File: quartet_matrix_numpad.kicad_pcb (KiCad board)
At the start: 2 copper layers, 100 x 100 mm, 34 parts

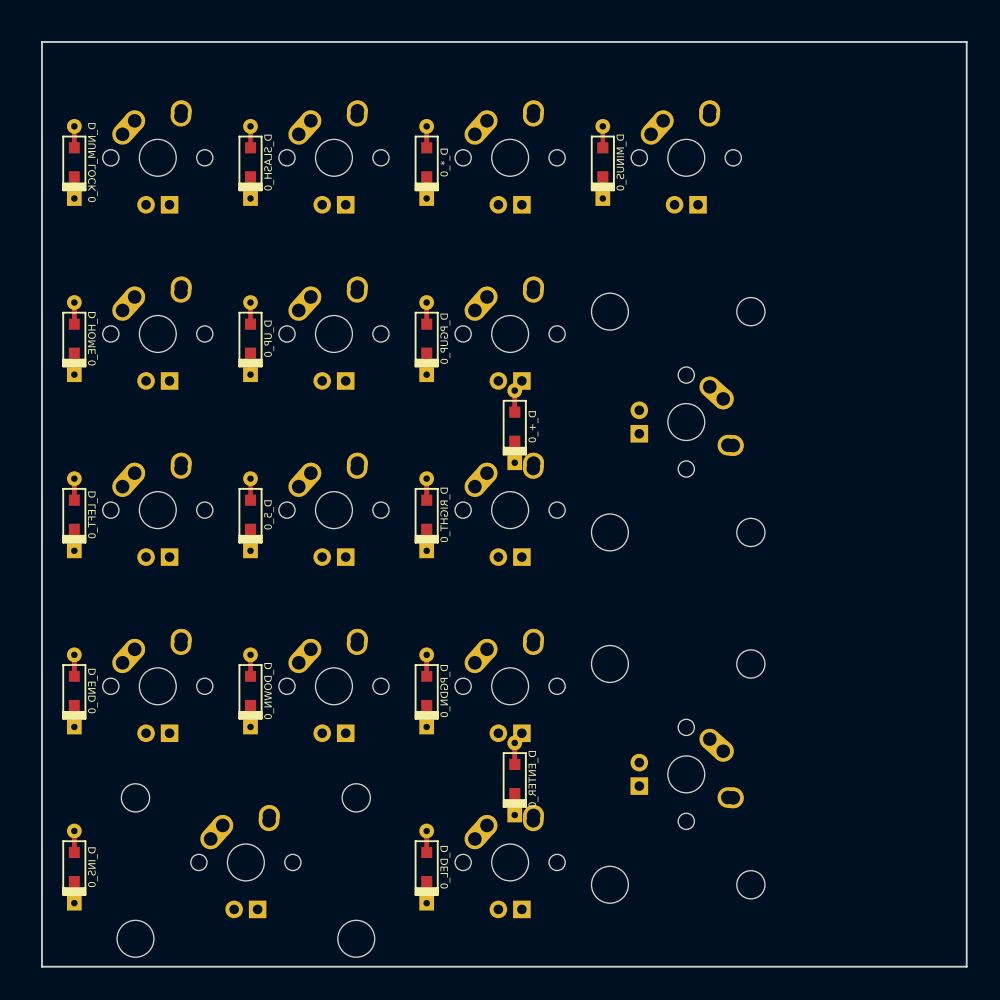
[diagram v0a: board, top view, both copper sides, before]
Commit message: Layout and route numpad matrix
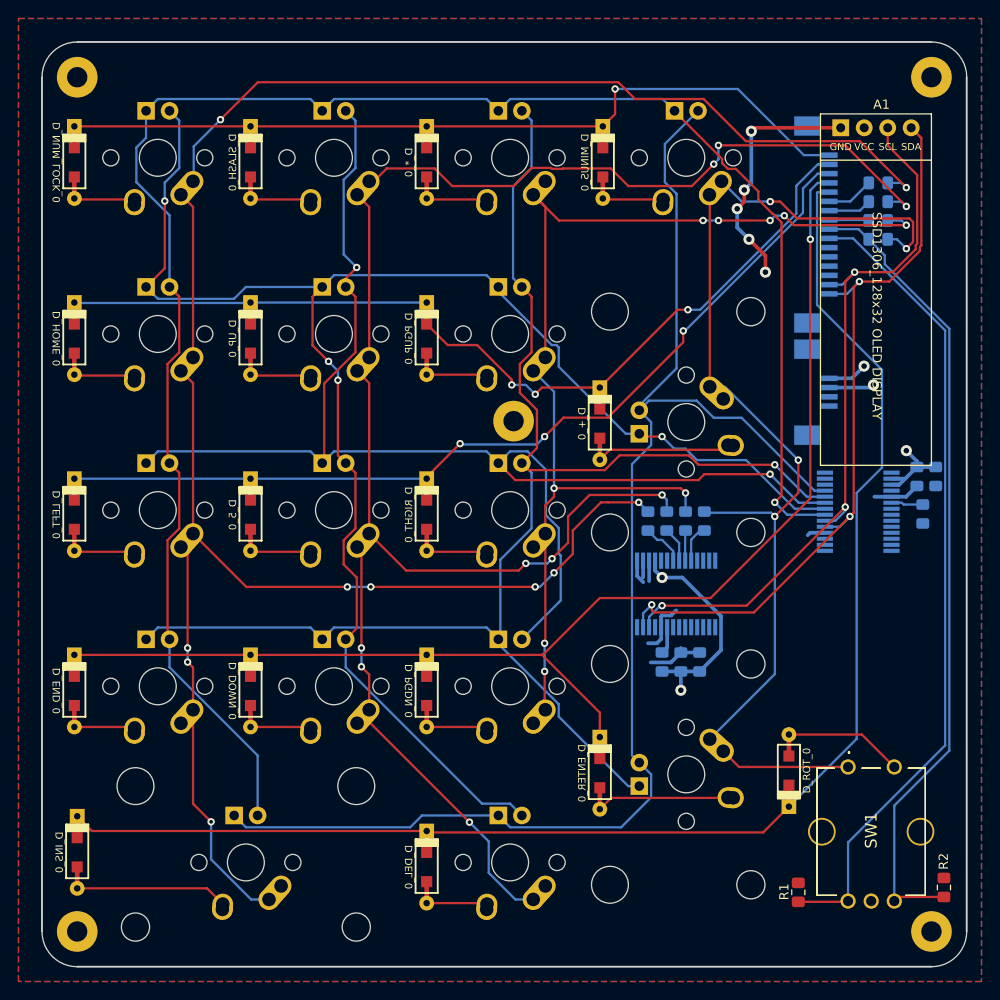
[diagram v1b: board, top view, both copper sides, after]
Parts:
- added A1: SSD1306_I2C_MODULE, Gigahawk:SSD1306_MODULE_128x32, F.Cu at (84.2, 7.78)
- added C1: 1u, Capacitor_SMD:C_0805_2012Metric_Pad1.15x1.40mm_HandSolder, B.Cu at (69.1, 67.0)
- added C2: 0.1u, Capacitor_SMD:C_0805_2012Metric_Pad1.15x1.40mm_HandSolder, B.Cu at (71.1, 67.0)
- added C3: 1u, Capacitor_SMD:C_0805_2012Metric_Pad1.15x1.40mm_HandSolder, B.Cu at (96.6, 47.0)
- added C4: 0.1u, Capacitor_SMD:C_0805_2012Metric_Pad1.15x1.40mm_HandSolder, B.Cu at (94.6, 47.0)
- added D_ROT_0: D, keyboard_parts:D_SOD123_axial, F.Cu at (80.8, 78.8)
- added H1: TopLeft(3.81,3.81), MountingHole:MountingHole_2.2mm_M2_Pad, F.Cu at (3.81, 3.81)
- added H2: TopRight(96.19,3.81), MountingHole:MountingHole_2.2mm_M2_Pad, F.Cu at (96.2, 3.81)
- added H3: BottomLeft(3.81,96.19), MountingHole:MountingHole_2.2mm_M2_Pad, F.Cu at (3.81, 96.2)
- added H4: BottomRight(96.19,96.19), MountingHole:MountingHole_2.2mm_M2_Pad, F.Cu at (96.2, 96.2)
- added H5: Center(51,41), MountingHole:MountingHole_2.2mm_M2_Pad, F.Cu at (51.0, 41.0)
- added H6: ConnectorPos(85.09,39.37), Gigahawk:DOT, F.Cu at (85.1, 39.4)
- added J2: QUARTET_RECV, Gigahawk:QUARTET_RECV_MATRIX, B.Cu at (85.1, 39.4)
- added R1: 20k, Resistor_SMD:R_0805_2012Metric_Pad1.15x1.40mm_HandSolder, F.Cu at (81.8, 92.0)
- added R10: DNI, Resistor_SMD:R_0805_2012Metric_Pad1.15x1.40mm_HandSolder, B.Cu at (90.4, 19.3)
- added R11: DNI, Resistor_SMD:R_0805_2012Metric_Pad1.15x1.40mm_HandSolder, B.Cu at (90.4, 21.3)
- added R12: 20k, Resistor_SMD:R_0805_2012Metric_Pad1.15x1.40mm_HandSolder, B.Cu at (95.2, 51.0)
- added R2: 20k, Resistor_SMD:R_0805_2012Metric_Pad1.15x1.40mm_HandSolder, F.Cu at (97.5, 91.4)
- added R3: 0R, Resistor_SMD:R_0805_2012Metric_Pad1.15x1.40mm_HandSolder, B.Cu at (67.1, 67.0)
- added R4: 0R, Resistor_SMD:R_0805_2012Metric_Pad1.15x1.40mm_HandSolder, B.Cu at (65.5, 51.8)
- added R5: 0R, Resistor_SMD:R_0805_2012Metric_Pad1.15x1.40mm_HandSolder, B.Cu at (67.6, 51.8)
- added R6: 0R, Resistor_SMD:R_0805_2012Metric_Pad1.15x1.40mm_HandSolder, B.Cu at (69.6, 51.8)
- added R7: 0R, Resistor_SMD:R_0805_2012Metric_Pad1.15x1.40mm_HandSolder, B.Cu at (71.6, 51.8)
- added R8: DNI, Resistor_SMD:R_0805_2012Metric_Pad1.15x1.40mm_HandSolder, B.Cu at (90.4, 15.2)
- added R9: DNI, Resistor_SMD:R_0805_2012Metric_Pad1.15x1.40mm_HandSolder, B.Cu at (90.4, 17.3)
- added SW1: Rotary_Encoder_Switch, Gigahawk:482016514001, F.Cu at (89.7, 85.4)
- added U1: MCP23017_SS, Package_SO:SSOP-28_5.3x10.2mm_P0.65mm, B.Cu at (68.6, 59.7)
- added U2: IS31FL3731-SA, Package_SO:SSOP-28_5.3x10.2mm_P0.65mm, B.Cu at (88.3, 50.8)
- moved D_ENTER_0 9.22 mm to (60.3, 79.1), turned to 270 degrees
- moved D_+_0 9.21 mm to (60.3, 41.3), turned to 270 degrees
- moved D_INS_0 1.62 mm to (3.81, 87.6), turned to 270 degrees
- turned D_*_0 to 270 degrees
- turned D_5_0 to 270 degrees
- turned D_DEL_0 to 270 degrees
- turned D_DOWN_0 to 270 degrees
- turned D_END_0 to 270 degrees
- turned D_HOME_0 to 270 degrees
- turned D_LEFT_0 to 270 degrees
- turned D_MINUS_0 to 270 degrees
- turned D_NUM_LOCK_0 to 270 degrees
- turned D_PGDN_0 to 270 degrees
- turned D_PGUP_0 to 270 degrees
- turned D_RIGHT_0 to 270 degrees
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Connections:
- net row0 renamed PD0
- net row1 renamed PD1
- net row2 renamed PD5
- net row3 renamed PD6
- net row4 renamed PD7
- K_*_0 pad 3: Net-(K_*_0-Pad3) -> CA4
- K_*_0 pad 4: Net-(K_*_0-Pad4) -> CA1
- K_+_0 pad 1: col3 -> ROT_S2
- K_+_0 pad 3: Net-(K_+_0-Pad3) -> CA5
- K_+_0 pad 4: Net-(K_+_0-Pad4) -> CA2
- K_5_0 pad 3: Net-(K_5_0-Pad3) -> CA2
- K_5_0 pad 4: Net-(K_5_0-Pad4) -> CA3
- K_DEL_0 pad 3: Net-(K_DEL_0-Pad3) -> CA2
- K_DEL_0 pad 4: Net-(K_DEL_0-Pad4) -> CA5
- K_DOWN_0 pad 3: Net-(K_DOWN_0-Pad3) -> CA2
- K_DOWN_0 pad 4: Net-(K_DOWN_0-Pad4) -> CA4
- K_END_0 pad 3: Net-(K_END_0-Pad3) -> CA1
- K_END_0 pad 4: Net-(K_END_0-Pad4) -> CA4
- K_ENTER_0 pad 1: Net-(K_ENTER_0-Pad1) -> ROT_S2
- K_ENTER_0 pad 3: Net-(K_ENTER_0-Pad3) -> CA5
- K_ENTER_0 pad 4: Net-(K_ENTER_0-Pad4) -> CA4
- K_HOME_0 pad 3: Net-(K_HOME_0-Pad3) -> CA1
- K_HOME_0 pad 4: Net-(K_HOME_0-Pad4) -> CA2
- K_INS_0 pad 3: Net-(K_INS_0-Pad3) -> CA1
- K_INS_0 pad 4: Net-(K_INS_0-Pad4) -> CA5
- K_LEFT_0 pad 3: Net-(K_LEFT_0-Pad3) -> CA1
- K_LEFT_0 pad 4: Net-(K_LEFT_0-Pad4) -> CA3
- K_MINUS_0 pad 1: col3 -> ROT_S2
- K_MINUS_0 pad 3: Net-(K_MINUS_0-Pad3) -> CA5
- K_MINUS_0 pad 4: Net-(K_MINUS_0-Pad4) -> CA1
- K_NUM_LOCK_0 pad 3: Net-(K_NUM_LOCK_0-Pad3) -> CA2
- K_NUM_LOCK_0 pad 4: Net-(K_NUM_LOCK_0-Pad4) -> CA1
- K_PGDN_0 pad 3: Net-(K_PGDN_0-Pad3) -> CA3
- K_PGDN_0 pad 4: Net-(K_PGDN_0-Pad4) -> CA4
- K_PGUP_0 pad 3: Net-(K_PGUP_0-Pad3) -> CA4
- K_PGUP_0 pad 4: Net-(K_PGUP_0-Pad4) -> CA2
- K_RIGHT_0 pad 3: Net-(K_RIGHT_0-Pad3) -> CA4
- K_RIGHT_0 pad 4: Net-(K_RIGHT_0-Pad4) -> CA3
- K_SLASH_0 pad 3: Net-(K_SLASH_0-Pad3) -> CA3
- K_SLASH_0 pad 4: Net-(K_SLASH_0-Pad4) -> CA1
- K_UP_0 pad 3: Net-(K_UP_0-Pad3) -> CA3
- K_UP_0 pad 4: Net-(K_UP_0-Pad4) -> CA2
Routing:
- net col0: track 0.00 -> 227.4 mm, vias 0 -> 10
- net CA1: track 0.00 -> 198.9 mm, vias 0 -> 1
- net col1: track 0.00 -> 192.6 mm, vias 0 -> 9
- net CA2: track 0.00 -> 178.7 mm, vias 0 -> 4
- net CA4: track 0.00 -> 161.8 mm, vias 0 -> 1
- net PD7: track 0.00 -> 153.6 mm
- net CA5: track 0.00 -> 152.7 mm
- net CA3: track 0.00 -> 147.1 mm, vias 0 -> 2
- net PD6: track 0.00 -> 133.7 mm, vias 0 -> 1
- net col2: track 0.00 -> 119.0 mm, vias 0 -> 9
- net ROT_S2: track 0.00 -> 118.0 mm, vias 0 -> 4
- net PD5: track 0.00 -> 97.7 mm, vias 0 -> 3
- net PD1: track 0.00 -> 97.2 mm, vias 0 -> 3
- net PC3: track 0.00 -> 88.2 mm
- net PC2: track 0.00 -> 88.0 mm
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- added copper zone on F.Cu, net +5V
- added copper zone on B.Cu, net GND
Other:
- outline, holes or cut-outs redrawn

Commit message: Reroute matrix, redo schematics for feather compat
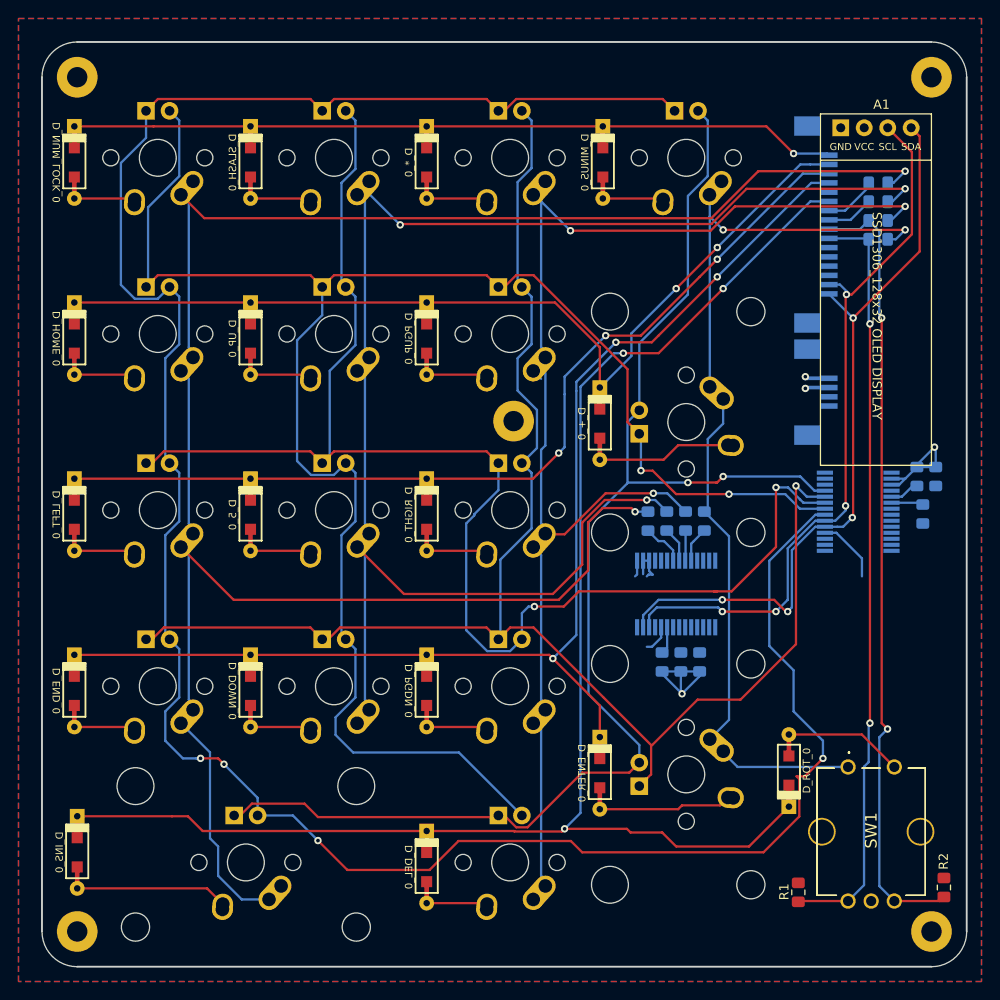
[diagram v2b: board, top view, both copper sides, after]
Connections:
- net ADC7 renamed SPARE
- net PD0 renamed D0
- net PD1 renamed D1
- net PD5 renamed D2
- net PD6 renamed D3
- A1 pad 2: +5V -> +3V3
- C1 pad 1: +5V -> +3V3
- C2 pad 1: +5V -> +3V3
- C3 pad 1: +5V -> +3V3
- C4 pad 1: +5V -> +3V3
- D_DEL_0 pad 1: PD7 -> A1
- D_INS_0 pad 1: PD7 -> A1
- D_ROT_0 pad 1: PD7 -> A1
- J2 pad 10: PC3 -> A5
- J2 pad 17: +5V -> +3V3
- J2 pad 18: +5V -> +3V3
- J2 pad 5: PD7 -> A0
- J2 pad 6: PB0 -> A1
- J2 pad 7: PB1 -> A2
- J2 pad 8: PB2 -> A3
- J2 pad 9: PC2 -> A4
- K_DEL_0 pad 1: col1 -> col2
- R1 pad 1: +5V -> +3V3
- R1 pad 2: PC3 -> A5
- R10 pad 1: PB2 -> A4
- R11 pad 1: PC2 -> A5
- R2 pad 1: PC2 -> A4
- R2 pad 2: +5V -> +3V3
- R3 pad 1: +5V -> +3V3
- R8 pad 1: PB0 -> A2
- R9 pad 1: PB1 -> A3
- SW1 pad A: PC3 -> A5
- SW1 pad B: PC2 -> A4
- U2 pad 2: +5V -> +3V3
- U2 pad 3: +5V -> +3V3
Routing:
- net A1: track 0.00 -> 164.2 mm, vias 0 -> 3
- net PD7: track 153.6 -> 0.00 mm
- net PC3: track 88.2 -> 0.00 mm
- net PC2: track 88.0 -> 0.00 mm
- net A4: track 0.00 -> 85.7 mm, vias 0 -> 2
- net A5: track 0.00 -> 82.4 mm, vias 0 -> 2
- net CA1: track 198.9 -> 258.9 mm, vias 1 -> 4
- net +5V: track 41.9 -> 0.00 mm, vias 5 -> 0
- net GND: track 52.8 -> 19.7 mm, vias 5 -> 0
- net +3V3: track 0.00 -> 30.4 mm, vias 0 -> 4
- net col1: track 192.6 -> 166.8 mm, vias 9 -> 3
- net col2: track 119.0 -> 140.9 mm, vias 9 -> 3
- net CA2: track 178.7 -> 195.5 mm, vias 4 -> 2
- net ROT_S2: track 118.0 -> 104.5 mm, vias 4 -> 2
- net CA4: track 161.8 -> 171.6 mm
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- added copper zone on F.Cu, net +3V3
- removed copper zone on F.Cu, net +5V

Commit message: Finish and route quartet mainboard
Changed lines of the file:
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@@
       (net 17 "Net-(D_DEL_0-Pad2)"))
   )
-  (gr_arc (start 3.81 3.81) (end 3.81 0) (angle -90) (layer Edge.Cuts) (width 0.1))
-  (gr_arc (start 3.81 96.19) (end 0 96.19) (angle -90) (layer Edge.Cuts) (width 0.1))
-  (gr_arc (start 96.19 96.19) (end 100 96.19) (angle 90) (layer Edge.Cuts) (width 0.1))
-  (gr_arc (start 96.19 3.81) (end 100 3.81) (angle -90) (layer Edge.Cuts) (width 0.1))
-  (gr_line (start 3.81 0) (end 96.19 0) (layer Edge.Cuts) (width 0.2))
-  (gr_line (start 100 3.81) (end 100 96.19) (layer Edge.Cuts) (width 0.2))
-  (gr_line (start 96.19 100) (end 3.81 100) (layer Edge.Cuts) (width 0.2))
-  (gr_line (start 0 96.19) (end 0 3.81) (layer Edge.Cuts) (width 0.2))
-  (gr_arc (start 91.725 0) (end 91.725 0) (angle 90) (layer Edge.Cuts) (width 0.2))
   (segment (start 9.925 16.925) (end 10.025 17.025) (width 0.25) (layer F.Cu) (net 1))
   (segment (start 3.5 16.925) (end 9.925 16.925) (width 0.25) (layer F.Cu) (net 1))
@@
     )
   )
+  (gr_line (start 3.810 0.000) (end 96.190 -0.000) (angle 90) (layer Edge.Cuts) (width 0.1))
+  (gr_line (start 100.000 3.810) (end 100.000 96.190) (angle 90) (layer Edge.Cuts) (width 0.1))
+  (gr_line (start 96.190 100.000) (end 3.810 100.000) (angle 90) (layer Edge.Cuts) (width 0.1))
+  (gr_line (start -0.000 96.190) (end 0.000 3.810) (angle 90) (layer Edge.Cuts) (width 0.1))
+  (gr_arc (start 3.810 3.810) (end 3.810 0.000) (angle -90.000) (layer Edge.Cuts) (width 0.1))
+  (gr_arc (start 3.810 96.190) (end -0.000 96.190) (angle -90.000) (layer Edge.Cuts) (width 0.1))
+  (gr_arc (start 96.190 96.190) (end 96.190 100.000) (angle -90.000) (layer Edge.Cuts) (width 0.1))
+  (gr_arc (start 96.190 3.810) (end 100.000 3.810) (angle -90.000) (layer Edge.Cuts) (width 0.1))
 )

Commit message: Get ready for JLCPCB
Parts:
- R1, R2: moved to B.Cu
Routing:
- net +3V3: track 30.4 -> 35.6 mm, vias 4 -> 6
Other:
- board text added: "JLCJLCJLCJLC"

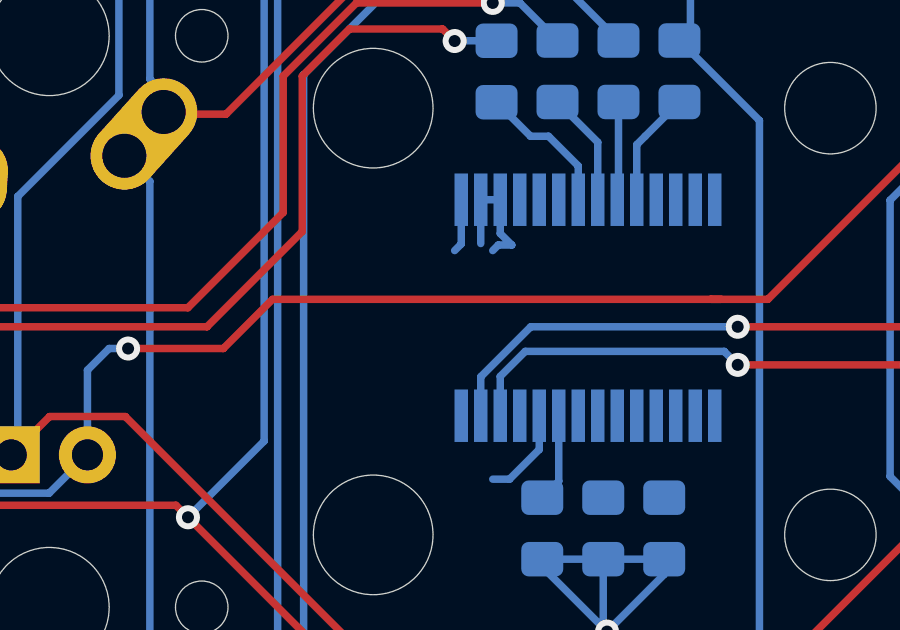
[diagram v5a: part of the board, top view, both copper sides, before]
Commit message: Fix unconnected IO expander reset
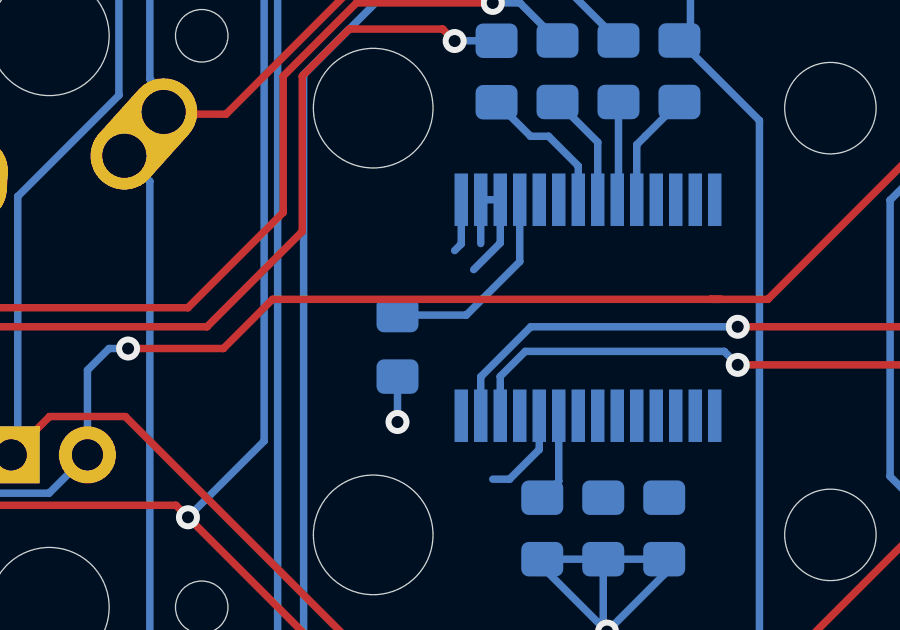
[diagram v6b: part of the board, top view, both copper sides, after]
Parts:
- added R13: 20k, Resistor_SMD:R_0805_2012Metric_Pad1.15x1.40mm_HandSolder, B.Cu at (62.2, 61.0)
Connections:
- U1 pad 18: +5V -> Net-(R13-Pad2)
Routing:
- net Net-(R13-Pad2): track 0.00 -> 6.88 mm
- net +3V3: track 35.6 -> 37.1 mm, vias 6 -> 7
